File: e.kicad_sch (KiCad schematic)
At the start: 9 parts, among them SW1 usr, SW2 rst, U1 Display_ST7789, U2 MAX98357A

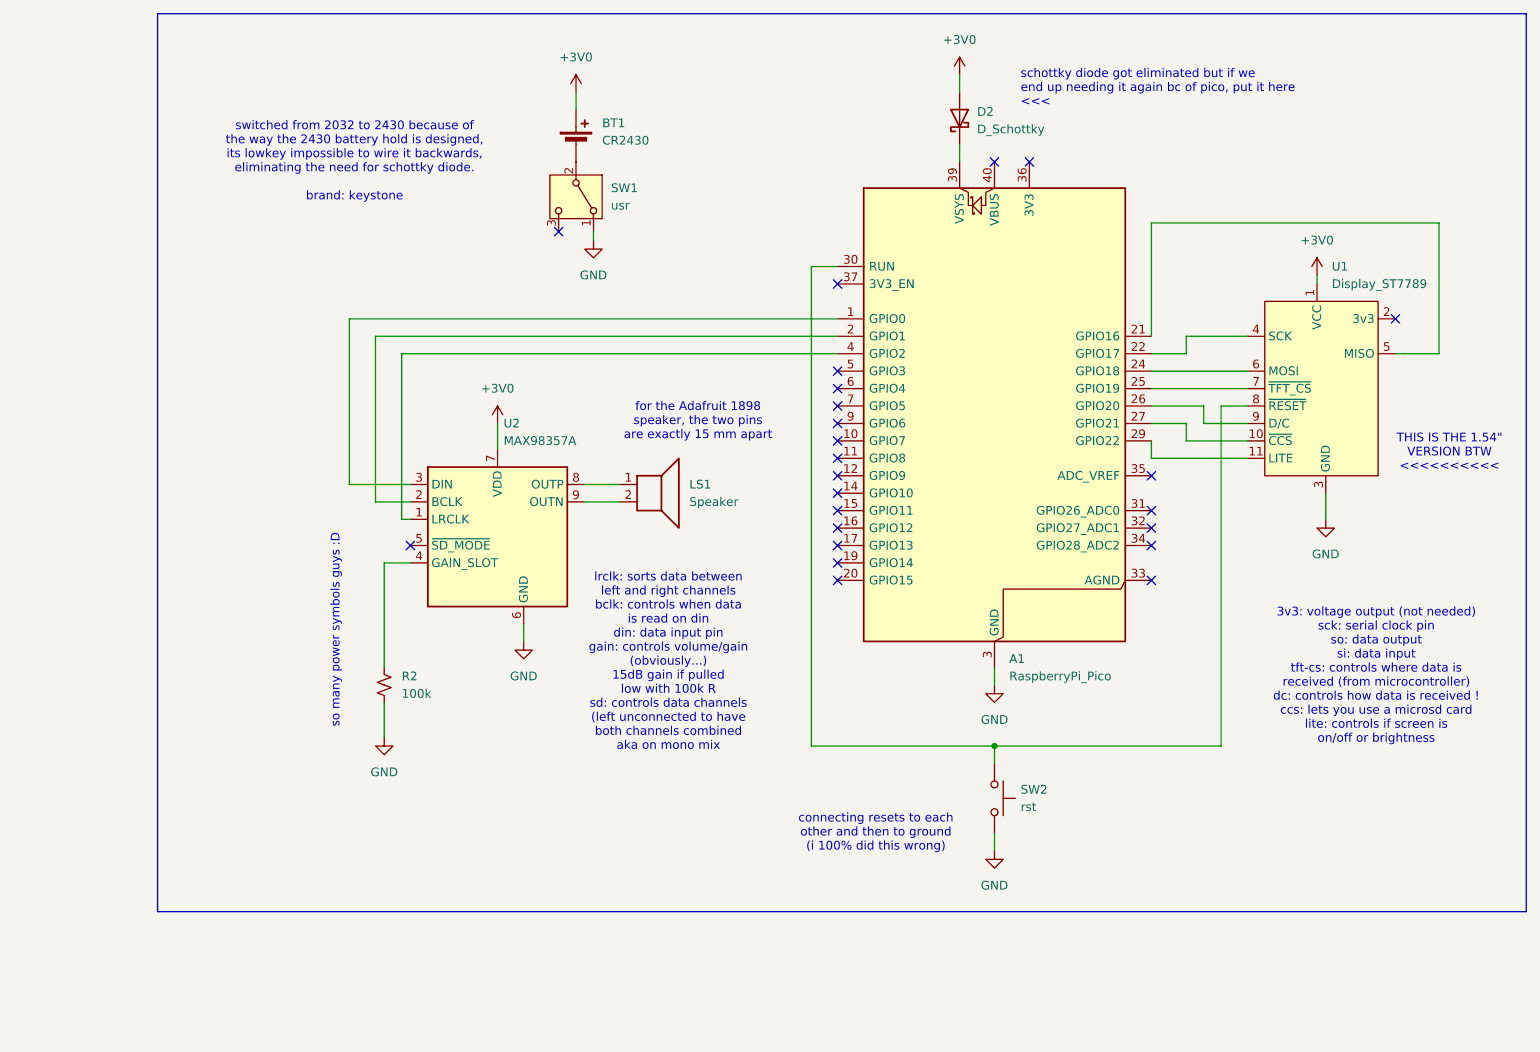
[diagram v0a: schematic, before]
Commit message: minor schematic cosmetic changes, cleaned up a few traces on PCB
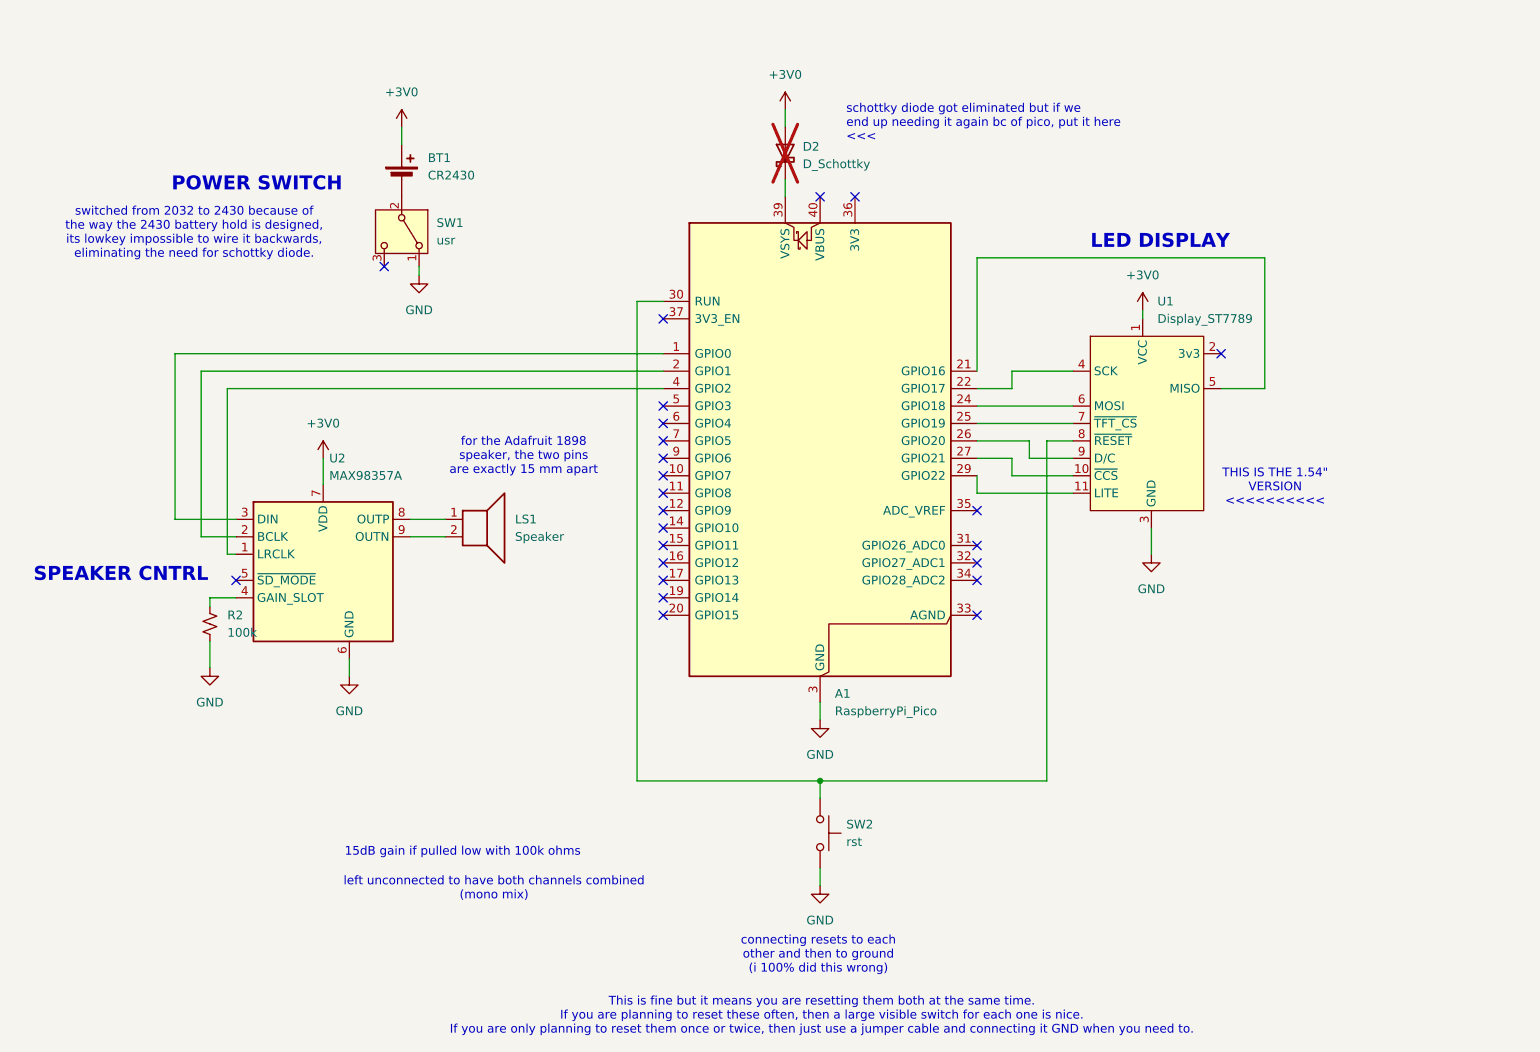
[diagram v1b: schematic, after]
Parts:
- D2: now not fitted; now left out of the parts list
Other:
- note added: "15dB gain if pulled low with 100k ohms"
- note added: "LED DISPLAY"
- note added: "POWER SWITCH"
- note added: "SPEAKER CNTRL"
- note added: "THIS IS THE 1.54" VERSION <<<<<<<<<<"
- note added: "This is fine but it means you are resetting them both at the same time. If you are planning to reset these often, then a large visible switch for each one is nice. If you are only planning to reset them once or twice, then just use a jumper cable and connecting it GND when you need to."
- note added: "left unconnected to have both channels combined (mono mix)"
- note added: "switched from 2032 to 2430 because of the way the 2430 battery hold is designed, its lowkey impossible to wire it backwards, eliminating the need for schottky diode."
- note removed: "3v3: voltage output (not needed) sck: serial clock pin so: data output si: data input tft-cs: controls where data is received (from microcontroller) dc: controls how data is received ! ccs: lets you use a microsd card lite: controls if screen is on/off or brightness"
- note removed: "THIS IS THE 1.54" VERSION BTW <<<<<<<<<<"
- note removed: "lrclk: sorts data between left and right channels bclk: controls when data is read on din din: data input pin gain: controls volume/gain (obviously...) 15dB gain if pulled low with 100k R sd: controls data channels (left unconnected to have both channels combined aka on mono mix"
- note removed: "so many power symbols guys :D"
- note removed: "switched from 2032 to 2430 because of the way the 2430 battery hold is designed, its lowkey impossible to wire it backwards, eliminating the need for schottky diode. brand: keystone"
- moved on the sheet: A1, BT1, LS1, R2, SW1, SW2, U1, U2
